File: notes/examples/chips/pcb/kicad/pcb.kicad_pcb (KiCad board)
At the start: 2 copper layers, 28.7 x 27.1 mm, 12 parts, among them J1 BOOT, J2 UART, SW1 BOOT, SW2 USER, U1 STM32F103C8Tx, U2 AMS1117-3.3

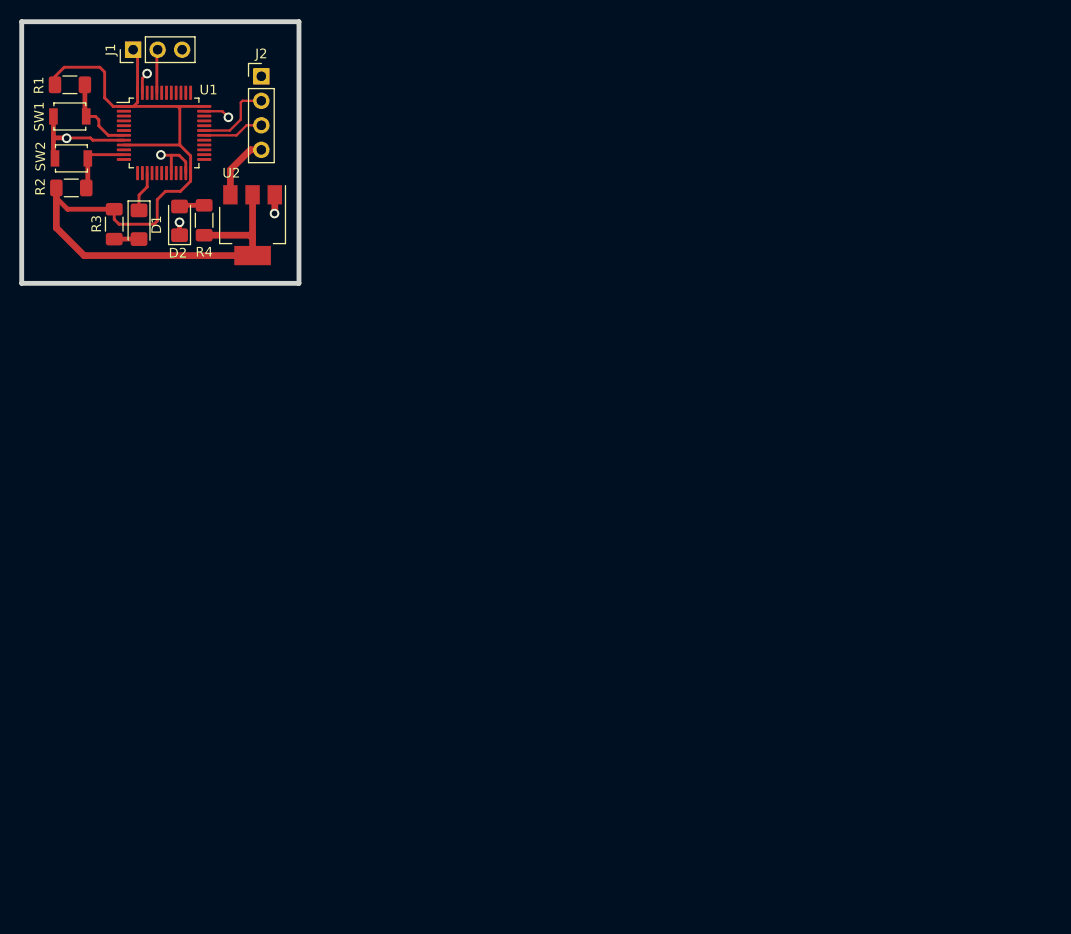
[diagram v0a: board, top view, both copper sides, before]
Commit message: Rework KiCAD Guide
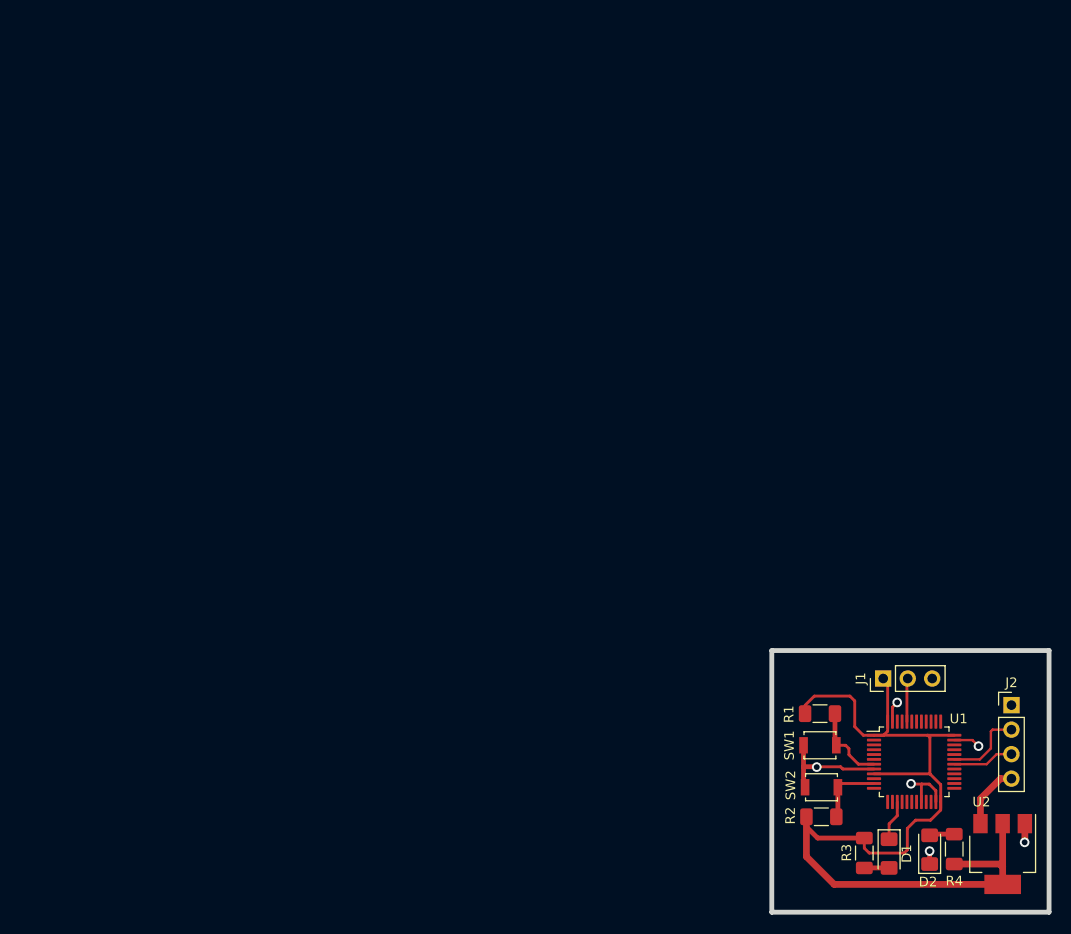
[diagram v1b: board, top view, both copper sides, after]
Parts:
- moved D1 101.5 mm to (148.8, 106.8)
- moved D2 101.5 mm to (153.0, 106.4)
- moved J1 101.5 mm to (148.2, 88.7)
- moved R2 101.5 mm to (141.8, 103.0)
- moved R4 101.5 mm to (155.6, 106.3)
- moved SW1 101.5 mm to (141.6, 95.6)
- moved U1 101.5 mm to (151.4, 97.3)
- moved J2 101.5 mm to (161.5, 91.4)
- moved R1 101.5 mm to (141.6, 92.3)
- moved SW2 101.5 mm to (141.8, 99.9)
- moved U2 101.5 mm to (160.6, 106.9)
- moved R3 101.5 mm to (146.2, 106.8)
